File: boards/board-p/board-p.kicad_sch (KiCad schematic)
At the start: 24 parts, among them J1 TYPE-C-31-M-17, J2 PogoPad_1x4_NVM_I2C, J3 PogoPad_1x8_Debug, Q1 AO3401A, U1 STUSB4500QTR

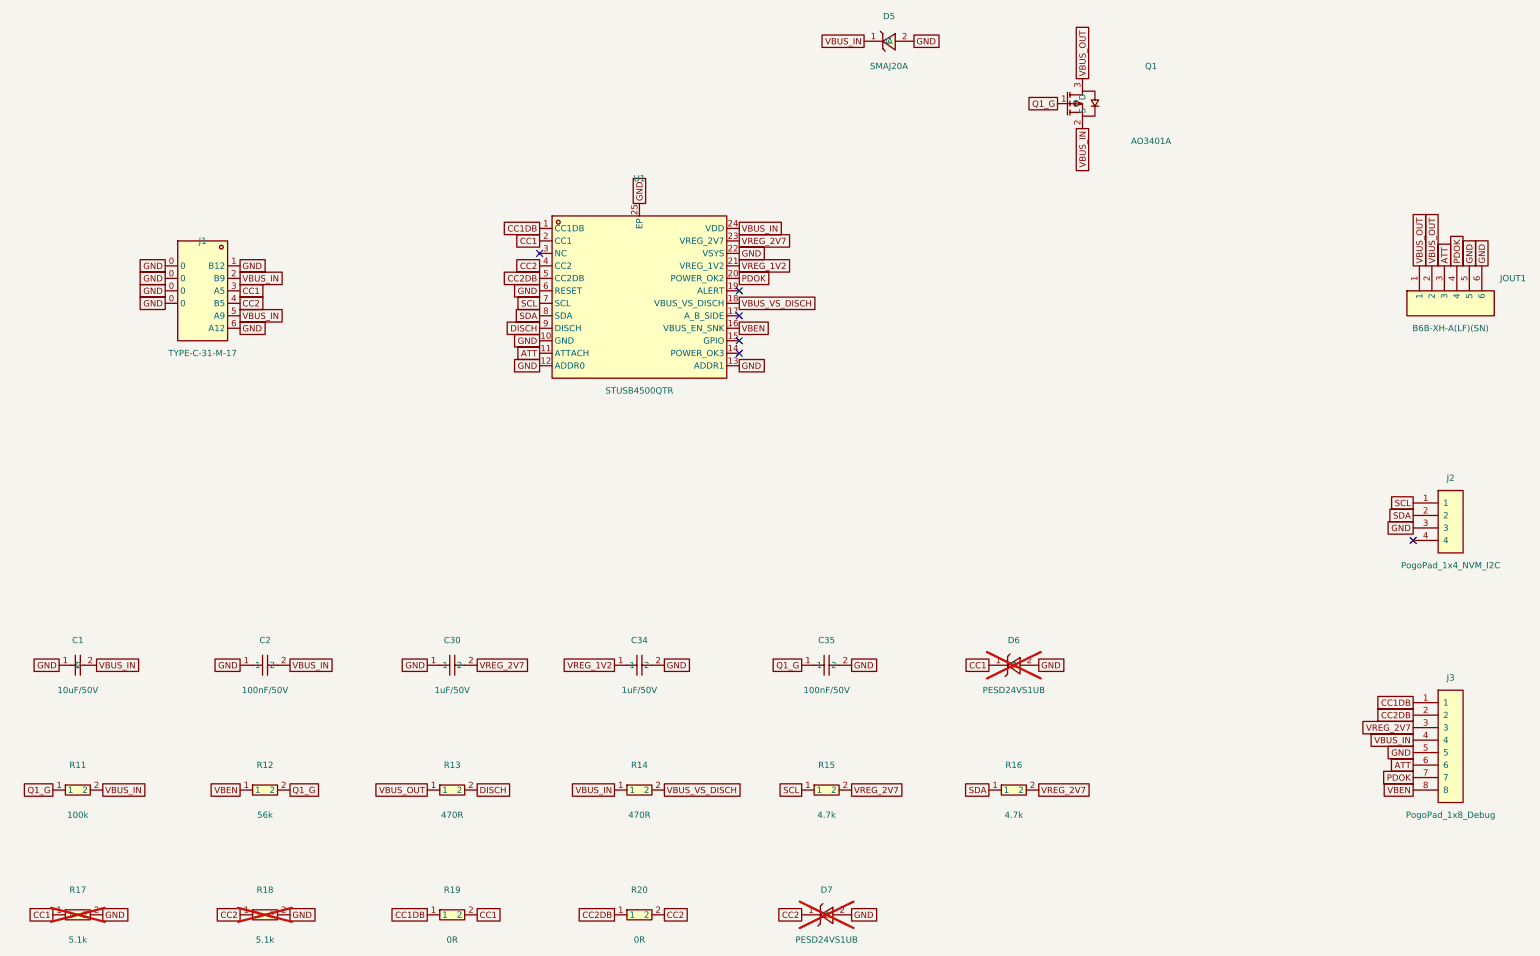
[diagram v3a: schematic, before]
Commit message: fix: apply design-review findings to both boards and docs
Independent electrical review (netlists confirmed pin-for-pin against
datasheets; three real problems found, all fixed before fab):

Board P:
- C35 soft-start re-referenced gate-to-SOURCE (VBUS_IN), not GND.
  Ground-referenced it let Q1 conduct ~16ms at every plug-in and slam
  on un-soft-started at the 5->15V contract step
- R12 56k -> 150k (C22807): old divider put VGS at -12.8V in a 20V
  mis-contract, over the AO3401A's +/-12V abs max; now -8.0V there
- U1.RESET now reaches GND via new R21 10k (C17414) and is brought
  out on J2.4 so the programming jig can recover a wedged NVM write

Board L:
- ballast R30-R37: 1206 250mW -> 2512 1W (C2934070) — the 1206 sat at
  107% of rating at the design's own worst-case 90mA string
- R27/R28 100R (C22775) in series with the encoder phases (contact
  protection for the C22/C23 debounce discharge)
- TP1 bare test pad on CTRL (Gates 3/4 both probe this node)

Docs updated to match: net tables, ratings, BOM (18 Extended lines now,
was 19), duty-cycle figures corrected to datasheet equations (~77%),
LED_P documented as a switching node with layout rules, pulse-skip
dimming-floor check added to Gate 4, R14/R21 open questions resolved
from primary datasheets. Both boards remain ERC-clean and
netlist-verified; doc site builds.

Co-Authored-By: Claude <noreply@anthropic.com>
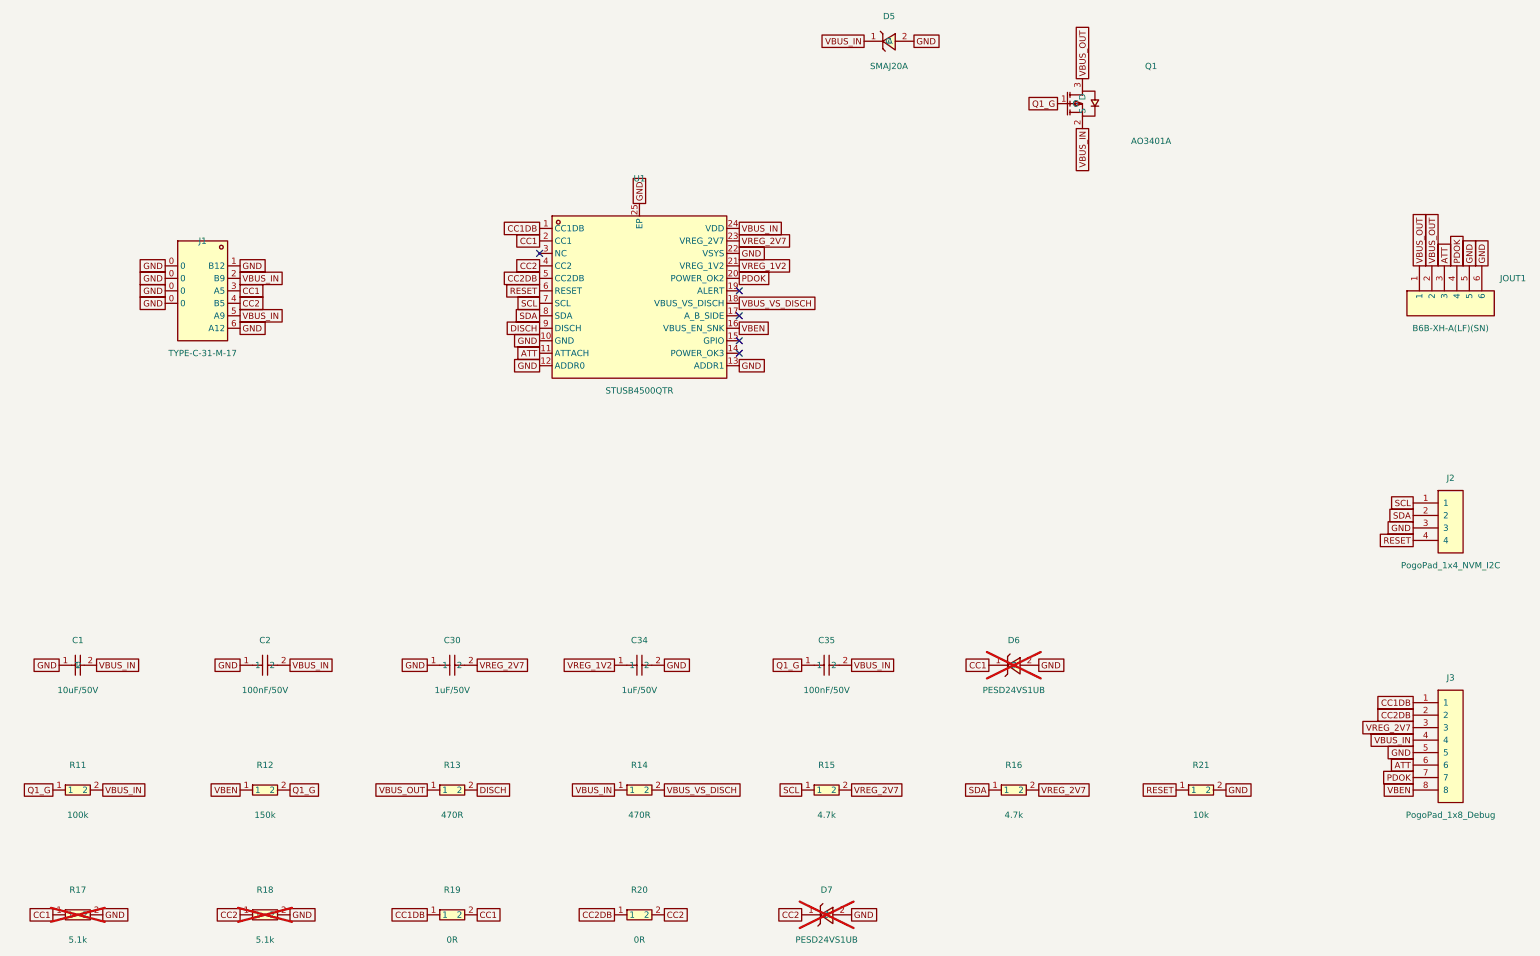
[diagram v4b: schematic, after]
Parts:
- removed R12: 56k, zudo-led-lamp:R0603, symbol zudo-led-lamp:0603WAF5602T5E
- added R12: 150k, zudo-led-lamp:R0603, symbol zudo-led-lamp:0603WAF1503T5E
- added R21: 10k, zudo-led-lamp:R0805, symbol zudo-led-lamp:0805W8F1002T5E
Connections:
- net GND: now also R21.2; no longer C35.2, U1.6 (RESET)
- net Q1_G: now also R12.2
- net VBEN: now also R12.1
- net VBUS_IN: now also C35.2
- net RESET: now reaches J2.4
- net RESET: now also U1.6 (RESET), R21.1
- no-connect marks 6 -> 5
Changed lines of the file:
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@@
 		(instances
 			(project "board-p"
-				(path "/ddc06ac7-b1ea-446f-805e-0151ddad6df9"
+				(path "/60b92f50-f594-4bac-a491-398955251f2a"
 					(reference "J1")
 					(unit 1)
@@
 		(instances
 			(project "board-p"
-				(path "/ddc06ac7-b1ea-446f-805e-0151ddad6df9"
+				(path "/60b92f50-f594-4bac-a491-398955251f2a"
 					(reference "U1")
 					(unit 1)
@@
 		(instances
 			(project "board-p"
-				(path "/ddc06ac7-b1ea-446f-805e-0151ddad6df9"
+				(path "/60b92f50-f594-4bac-a491-398955251f2a"
 					(reference "Q1")
 					(unit 1)
@@
 		(instances
 			(project "board-p"
-				(path "/ddc06ac7-b1ea-446f-805e-0151ddad6df9"
+				(path "/60b92f50-f594-4bac-a491-398955251f2a"
 					(reference "D5")
 					(unit 1)
@@
 		(instances
 			(project "board-p"
-				(path "/ddc06ac7-b1ea-446f-805e-0151ddad6df9"
+				(path "/60b92f50-f594-4bac-a491-398955251f2a"
 					(reference "D6")
 					(unit 1)
@@
 		(instances
 			(project "board-p"
-				(path "/ddc06ac7-b1ea-446f-805e-0151ddad6df9"
+				(path "/60b92f50-f594-4bac-a491-398955251f2a"
 					(reference "D7")
 					(unit 1)
@@
 		(instances
 			(project "board-p"
-				(path "/ddc06ac7-b1ea-446f-805e-0151ddad6df9"
+				(path "/60b92f50-f594-4bac-a491-398955251f2a"
 					(reference "C1")
 					(unit 1)
@@
 		(instances
 			(project "board-p"
-				(path "/ddc06ac7-b1ea-446f-805e-0151ddad6df9"
+				(path "/60b92f50-f594-4bac-a491-398955251f2a"
 					(reference "C2")
 					(unit 1)
@@
 		(instances
 			(project "board-p"
-				(path "/ddc06ac7-b1ea-446f-805e-0151ddad6df9"
+				(path "/60b92f50-f594-4bac-a491-398955251f2a"
 					(reference "C30")
 					(unit 1)
@@
 		(instances
 			(project "board-p"
-				(path "/ddc06ac7-b1ea-446f-805e-0151ddad6df9"
+				(path "/60b92f50-f594-4bac-a491-398955251f2a"
 					(reference "C34")
 					(unit 1)
@@
 		(instances
 			(project "board-p"
-				(path "/ddc06ac7-b1ea-446f-805e-0151ddad6df9"
+				(path "/60b92f50-f594-4bac-a491-398955251f2a"
 					(reference "C35")
 					(unit 1)
@@
 		(instances
 			(project "board-p"
-				(path "/ddc06ac7-b1ea-446f-805e-0151ddad6df9"
+				(path "/60b92f50-f594-4bac-a491-398955251f2a"
 					(reference "R11")
 					(unit 1)
@@
 	)
 	(symbol
-		(lib_id "zudo-led-lamp:0603WAF5602T5E")
+		(lib_id "zudo-led-lamp:0603WAF1503T5E")
 		(at 76.2 190.5 0)
 		(unit 1)
@@
 			)
 		)
-		(property "Value" "56k"
+		(property "Value" "150k"
 			(at 76.2 195.58 0)
 			(effects
@@
 			)
 		)
-		(property "LCSC" "C23206"
+		(property "LCSC" "C22807"
 			(at 76.2 198.12 0)
 			(effects
@@
 		(instances
 			(project "board-p"
-				(path "/ddc06ac7-b1ea-446f-805e-0151ddad6df9"
+				(path "/60b92f50-f594-4bac-a491-398955251f2a"
 					(reference "R12")
 					(unit 1)
@@
 		(instances
 			(project "board-p"
-				(path "/ddc06ac7-b1ea-446f-805e-0151ddad6df9"
+				(path "/60b92f50-f594-4bac-a491-398955251f2a"
 					(reference "R13")
 					(unit 1)
@@
 		(instances
 			(project "board-p"
-				(path "/ddc06ac7-b1ea-446f-805e-0151ddad6df9"
+				(path "/60b92f50-f594-4bac-a491-398955251f2a"
 					(reference "R14")
 					(unit 1)
@@
 		(instances
 			(project "board-p"
-				(path "/ddc06ac7-b1ea-446f-805e-0151ddad6df9"
+				(path "/60b92f50-f594-4bac-a491-398955251f2a"
 					(reference "R15")
 					(unit 1)
@@
 		(instances
 			(project "board-p"
-				(path "/ddc06ac7-b1ea-446f-805e-0151ddad6df9"
+				(path "/60b92f50-f594-4bac-a491-398955251f2a"
 					(reference "R16")
 					(unit 1)
@@
 		(instances
 			(project "board-p"
-				(path "/ddc06ac7-b1ea-446f-805e-0151ddad6df9"
+				(path "/60b92f50-f594-4bac-a491-398955251f2a"
 					(reference "R17")
 					(unit 1)
@@
 		(instances
 			(project "board-p"
-				(path "/ddc06ac7-b1ea-446f-805e-0151ddad6df9"
+				(path "/60b92f50-f594-4bac-a491-398955251f2a"
 					(reference "R18")
 					(unit 1)
@@
 		(instances
 			(project "board-p"
-				(path "/ddc06ac7-b1ea-446f-805e-0151ddad6df9"
+				(path "/60b92f50-f594-4bac-a491-398955251f2a"
 					(reference "R19")
 					(unit 1)
@@
 		(instances
 			(project "board-p"
-				(path "/ddc06ac7-b1ea-446f-805e-0151ddad6df9"
+				(path "/60b92f50-f594-4bac-a491-398955251f2a"
 					(reference "R20")
+					(unit 1)
+				)
+			)
+		)
+	)
+	(symbol
+		(lib_id "zudo-led-lamp:0805W8F1002T5E")
+		(at 266.7 190.5 0)
+		(unit 1)
+		(exclude_from_sim no)
+		(in_bom yes)
+		(on_board yes)
+		(dnp no)
+		(property "Reference" "R21"
+			(at 266.7 185.42 0)
+			(effects
+				(font (size 1.27 1.27))
+			)
+		)
+		(property "Value" "10k"
+			(at 266.7 195.58 0)
+			(effects
+				(font (size 1.27 1.27))
+			)
+		)
+		(property "Footprint" "zudo-led-lamp:R0805"
+			(at 266.7 190.5 0)
+			(effects
+				(font (size 1.27 1.27))
+				(hide yes)
+			)
+		)
+		(property "Datasheet" ""
+			(at 266.7 190.5 0)
+			(effects
+				(font (size 1.27 1.27))
+				(hide yes)
+			)
+		)
+		(property "LCSC" "C17414"
+			(at 266.7 198.12 0)
+			(effects
+				(font (size 1.27 1.27))
+				(hide yes)
+			)
+		)
+		(pin "1"
+		)
+		(pin "2"
+		)
+		(instances
+			(project "board-p"
+				(path "/60b92f50-f594-4bac-a491-398955251f2a"
+					(reference "R21")
 					(unit 1)
 				)
@@
 		(instances
 			(project "board-p"
-				(path "/ddc06ac7-b1ea-446f-805e-0151ddad6df9"
+				(path "/60b92f50-f594-4bac-a491-398955251f2a"
 					(reference "JOUT1")
 					(unit 1)
@@
 		(instances
 			(project "board-p"
-				(path "/ddc06ac7-b1ea-446f-805e-0151ddad6df9"
+				(path "/60b92f50-f594-4bac-a491-398955251f2a"
 					(reference "J2")
 					(unit 1)
@@
 		(instances
 			(project "board-p"
-				(path "/ddc06ac7-b1ea-446f-805e-0151ddad6df9"
+				(path "/60b92f50-f594-4bac-a491-398955251f2a"
 					(reference "J3")
 					(unit 1)
@@
 		)
 	)
+	(global_label "VBUS_IN"
+		(shape passive)
+		(at 195.58 165.1 0)
+		(effects
+			(font (size 1.27 1.27))
+			(justify left)
+		)
+	)
 	(global_label "CC1"
 		(shape passive)
@@
 		)
 	)
+	(global_label "RESET"
+		(shape passive)
+		(at 132.08 88.9 180)
+		(effects
+			(font (size 1.27 1.27))
+			(justify right)
+		)
+	)
+	(global_label "RESET"
+		(shape passive)
+		(at 261.62 190.5 180)
+		(effects
+			(font (size 1.27 1.27))
+			(justify right)
+		)
+	)
+	(global_label "RESET"
+		(shape passive)
+		(at 309.88 139.7 180)
+		(effects
+			(font (size 1.27 1.27))
+			(justify right)
+		)
+	)
 	(global_label "ATT"
 		(shape passive)
@@
 	(global_label "GND"
 		(shape passive)
-		(at 132.08 88.9 180)
-		(effects
-			(font (size 1.27 1.27))
-			(justify right)
-		)
-	)
-	(global_label "GND"
-		(shape passive)
 		(at 132.08 104.14 180)
 		(effects
@@
 	(global_label "GND"
 		(shape passive)
-		(at 195.58 165.1 0)
+		(at 271.78 190.5 0)
 		(effects
 			(font (size 1.27 1.27))
@@
 		(at 172.72 88.9)
 	)
-	(no_connect
-		(at 309.88 139.7)
-	)
 	(sheet_instances
